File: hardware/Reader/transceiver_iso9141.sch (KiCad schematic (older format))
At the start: 8 parts

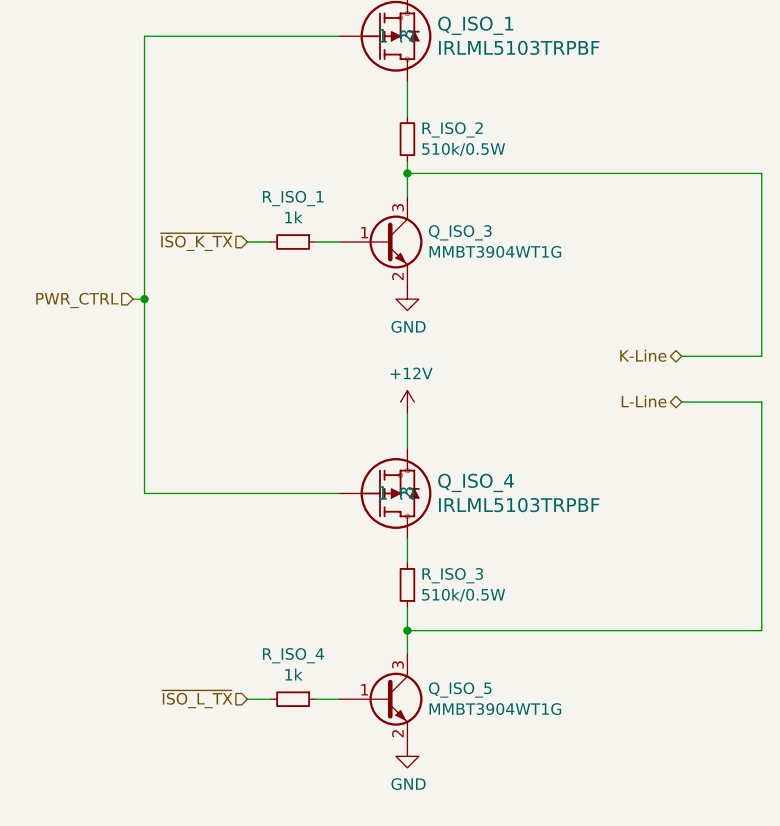
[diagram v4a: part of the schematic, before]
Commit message: Fixed bugs on the reader schematic. Exported Schematic Electrical report
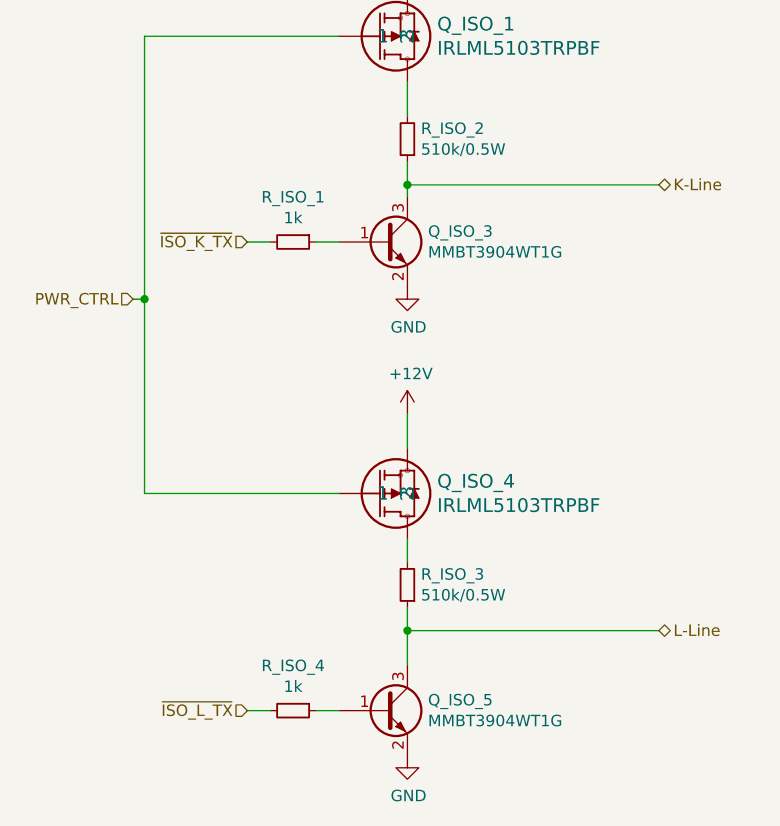
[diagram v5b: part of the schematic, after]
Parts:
- Q_ISO_1, Q_ISO_4: Manufacturer (none) -> Infineon Technologies; Part Name (none) -> IRLML5103TRPBF; Vendor (none) -> DigiKey Canada; digikeypn (none) -> IRLML5103PBFCT-ND
- Q_ISO_3, Q_ISO_5: Manufacturer (none) -> ON Semiconductor; Part Name (none) -> MMBT3904WT1G; Vendor (none) -> DigiKey Canada; digikeypn (none) -> MMBT3904WT1GOSCT-ND
- R_ISO_1, R_ISO_4: Manufacturer (none) -> Samsung Electro-Mechanics; Vendor (none) -> DigiKey Canada; digikeypn (none) -> 1276-3484-1-ND
- R_ISO_2, R_ISO_3: Manufacturer (none) -> Panasonic Electronic Components; Vendor (none) -> DigiKey Canada; digikeypn (none) -> P510KADCT-ND
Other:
- moved on the sheet: Q_ISO_5, R_ISO_4
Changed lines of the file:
@@
 $EndDescr
-Wire Wire Line
-	4450 2250 5300 2250
-Wire Wire Line
-	4450 3400 4450 2250
-Wire Wire Line
-	4400 3400 4450 3400
 Wire Wire Line
 	5600 2050 5600 1900
@@
 $EndComp
 Wire Wire Line
-	5600 2800 5600 2850
-Wire Wire Line
 	5600 2600 5600 2450
 $Comp
@@
 F 3 "https://industrial.panasonic.com/cdbs/www-data/pdf/RDO0000/AOA0000C331.pdf" H 5600 2700 50  0001 C CNN
 F 4 "ERJ-P06J514V" H 5600 2700 50  0001 C CNN "Part Name"
+F 5 "DigiKey Canada" H 5600 2700 50  0001 C CNN "Vendor"
+F 6 "Panasonic Electronic Components" H 5600 2700 50  0001 C CNN "Manufacturer"
+F 7 "P510KADCT-ND" H 5600 2700 50  0001 C CNN "digikeypn"
 	1    5600 2700
 	-1   0    0    1
@@
 F 3 "https://media.digikey.com/pdf/Data%20Sheets/Samsung%20PDFs/RC_Series_ds.pdf" H 5100 3150 50  0001 C CNN
 F 4 "RC1608F102CS" H 5100 3150 50  0001 C CNN "Part Name"
+F 5 "Samsung Electro-Mechanics" H 5100 3150 50  0001 C CNN "Manufacturer"
+F 6 "DigiKey Canada" H 5100 3150 50  0001 C CNN "Vendor"
+F 7 "1276-3484-1-ND" H 5100 3150 50  0001 C CNN "digikeypn"
 	1    5100 3150
 	0    1    1    0
@@
 L power:GND #PWR0126
 U 1 1 5FA99780
-P 5600 5350
-F 0 "#PWR0126" H 5600 5100 50  0001 C CNN
-F 1 "GND" H 5605 5177 50  0000 C CNN
-F 2 "" H 5600 5350 50  0001 C CNN
-F 3 "" H 5600 5350 50  0001 C CNN
-	1    5600 5350
+P 5600 5400
+F 0 "#PWR0126" H 5600 5150 50  0001 C CNN
+F 1 "GND" H 5605 5227 50  0000 C CNN
+F 2 "" H 5600 5400 50  0001 C CNN
+F 3 "" H 5600 5400 50  0001 C CNN
+	1    5600 5400
 	1    0    0    -1
 $EndComp
@@
 L Transistor_BJT:MMBT3904 Q_ISO_5
 U 1 1 5FA953EB
-P 5500 5150
-F 0 "Q_ISO_5" H 5690 5196 50  0000 L CNN
-F 1 "MMBT3904WT1G" H 5690 5105 50  0000 L CNN
-F 2 "Package_TO_SOT_SMD:SOT-23" H 5700 5075 50  0001 L CIN
-F 3 "https://www.onsemi.com/pub/Collateral/MMBT3904WT1-D.PDF" H 5500 5150 50  0001 L CNN
-	1    5500 5150
+P 5500 5200
+F 0 "Q_ISO_5" H 5690 5246 50  0000 L CNN
+F 1 "MMBT3904WT1G" H 5690 5155 50  0000 L CNN
+F 2 "Package_TO_SOT_SMD:SOT-23" H 5700 5125 50  0001 L CIN
+F 3 "https://www.onsemi.com/pub/Collateral/MMBT3904WT1-D.PDF" H 5500 5200 50  0001 L CNN
+F 4 "MMBT3904WT1G" H 5500 5200 50  0001 C CNN "Part Name"
+F 5 "DigiKey Canada" H 5500 5200 50  0001 C CNN "Vendor"
+F 6 "ON Semiconductor" H 5500 5200 50  0001 C CNN "Manufacturer"
+F 7 "MMBT3904WT1GOSCT-ND" H 5500 5200 50  0001 C CNN "digikeypn"
+	1    5500 5200
 	1    0    0    -1
 $EndComp
@@
 F 2 "Package_TO_SOT_SMD:SOT-23" H 5700 3075 50  0001 L CIN
 F 3 "https://www.onsemi.com/pub/Collateral/MMBT3904WT1-D.PDF" H 5500 3150 50  0001 L CNN
+F 4 "MMBT3904WT1G" H 5500 3150 50  0001 C CNN "Part Name"
+F 5 "DigiKey Canada" H 5500 3150 50  0001 C CNN "Vendor"
+F 6 "ON Semiconductor" H 5500 3150 50  0001 C CNN "Manufacturer"
+F 7 "MMBT3904WT1GOSCT-ND" H 5500 3150 50  0001 C CNN "digikeypn"
 	1    5500 3150
 	1    0    0    -1
@@
 F 3 "https://industrial.panasonic.com/cdbs/www-data/pdf/RDO0000/AOA0000C331.pdf" H 5600 4650 50  0001 C CNN
 F 4 "ERJ-P06J514V" H 5600 4650 50  0001 C CNN "Part Name"
+F 5 "DigiKey Canada" H 5600 4650 50  0001 C CNN "Vendor"
+F 6 "Panasonic Electronic Components" H 5600 4650 50  0001 C CNN "Manufacturer"
+F 7 "P510KADCT-ND" H 5600 4650 50  0001 C CNN "digikeypn"
 	1    5600 4650
 	-1   0    0    1
@@
 F 1 "IRLML5103TRPBF" H 5730 4303 60  0000 L CNN
 F 2 "footprints:IRLML5103TRPBF" H 5750 3990 60  0001 C CNN
-F 3 "" H 5300 4250 60  0000 C CNN
+F 3 "https://www.infineon.com/dgdl/irlml5103pbf.pdf?fileId=5546d462533600a401535668505d2617" H 5300 4250 60  0001 C CNN
+F 4 "IRLML5103TRPBF" H 5300 4250 50  0001 C CNN "Part Name"
+F 5 "DigiKey Canada" H 5300 4250 50  0001 C CNN "Vendor"
+F 6 "Infineon Technologies" H 5300 4250 50  0001 C CNN "Manufacturer"
+F 7 "IRLML5103PBFCT-ND" H 5300 4250 50  0001 C CNN "digikeypn"
 	1    5300 4250
 	1    0    0    1
@@
 F 1 "IRLML5103TRPBF" H 5730 2303 60  0000 L CNN
 F 2 "footprints:IRLML5103TRPBF" H 5750 1990 60  0001 C CNN
-F 3 "" H 5300 2250 60  0000 C CNN
+F 3 "https://www.infineon.com/dgdl/irlml5103pbf.pdf?fileId=5546d462533600a401535668505d2617" H 5300 2250 60  0001 C CNN
+F 4 "IRLML5103TRPBF" H 5300 2250 50  0001 C CNN "Part Name"
+F 5 "DigiKey Canada" H 5300 2250 50  0001 C CNN "Vendor"
+F 6 "Infineon Technologies" H 5300 2250 50  0001 C CNN "Manufacturer"
+F 7 "IRLML5103PBFCT-ND" H 5300 2250 50  0001 C CNN "digikeypn"
 	1    5300 2250
 	1    0    0    1
@@
 Text HLabel 4900 3150 0    50   Input ~ 0
 ~ISO_K_TX~
+Text HLabel 4900 5200 0    50   Input ~ 0
+~ISO_L_TX~
+$Comp
+L Device:R_Small R_ISO_4
+U 1 1 5FAABEED
+P 5100 5200
+F 0 "R_ISO_4" V 4904 5200 50  0000 C CNN
+F 1 "1k" V 4995 5200 50  0000 C CNN
+F 2 "footprints:RC1608F102CS" H 5100 5200 50  0001 C CNN
+F 3 "https://media.digikey.com/pdf/Data%20Sheets/Samsung%20PDFs/RC_Series_ds.pdf" H 5100 5200 50  0001 C CNN
+F 4 "RC1608F102CS" H 5100 5200 50  0001 C CNN "Part Name"
+F 5 "Samsung Electro-Mechanics" H 5100 5200 50  0001 C CNN "Manufacturer"
+F 6 "DigiKey Canada" H 5100 5200 50  0001 C CNN "Vendor"
+F 7 "1276-3484-1-ND" H 5100 5200 50  0001 C CNN "digikeypn"
+	1    5100 5200
+	0    1    1    0
+$EndComp
+Wire Wire Line
+	4900 5200 5000 5200
+Wire Wire Line
+	5200 5200 5300 5200
+Text HLabel 6700 2900 2    50   BiDi ~ 0
+K-Line
+Text HLabel 6700 4850 2    50   BiDi ~ 0
+L-Line
+Wire Wire Line
+	5600 2800 5600 2900
+Wire Wire Line
+	5600 4750 5600 4850
+Wire Wire Line
+	5600 2900 6700 2900
+Connection ~ 5600 2900
+Wire Wire Line
+	5600 2900 5600 2950
+Wire Wire Line
+	5600 4850 6700 4850
+Connection ~ 5600 4850
+Wire Wire Line
+	5600 4850 5600 5000
+Wire Wire Line
+	4450 4250 5300 4250
+Wire Wire Line
+	4450 2250 5300 2250
+Wire Wire Line
+	4450 3400 4450 2250
+Wire Wire Line
+	4400 3400 4450 3400
 Text HLabel 4400 3400 0    50   Input ~ 0
 PWR_CTRL
-Connection ~ 5600 2850
-Wire Wire Line
-	5600 2850 5600 2950
 Wire Wire Line
 	4450 3400 4450 4250
-Wire Wire Line
-	4450 4250 5300 4250
 Connection ~ 4450 3400
-Text HLabel 4900 5150 0    50   Input ~ 0
-~ISO_L_TX~
-$Comp
-L Device:R_Small R_ISO_4
-U 1 1 5FAABEED
-P 5100 5150
-F 0 "R_ISO_4" V 4904 5150 50  0000 C CNN
-F 1 "1k" V 4995 5150 50  0000 C CNN
-F 2 "footprints:RC1608F102CS" H 5100 5150 50  0001 C CNN
-F 3 "https://media.digikey.com/pdf/Data%20Sheets/Samsung%20PDFs/RC_Series_ds.pdf" H 5100 5150 50  0001 C CNN
-F 4 "RC1608F102CS" H 5100 5150 50  0001 C CNN "Part Name"
-	1    5100 5150
-	0    1    1    0
-$EndComp
-Wire Wire Line
-	4900 5150 5000 5150
-Wire Wire Line
-	5200 5150 5300 5150
-Text HLabel 6800 3650 0    50   BiDi ~ 0
-K-Line
-Wire Wire Line
-	5600 2850 7150 2850
-Connection ~ 5600 4850
-Wire Wire Line
-	5600 4750 5600 4850
-Wire Wire Line
-	5600 4850 5600 4950
-Text HLabel 6800 3850 0    50   BiDi ~ 0
-L-Line
-Wire Wire Line
-	6800 3650 7150 3650
-Wire Wire Line
-	5600 4850 7150 4850
-Wire Wire Line
-	7150 3850 6800 3850
-Wire Wire Line
-	7150 4850 7150 3850
-Wire Wire Line
-	7150 3650 7150 2850
 $EndSCHEMATC

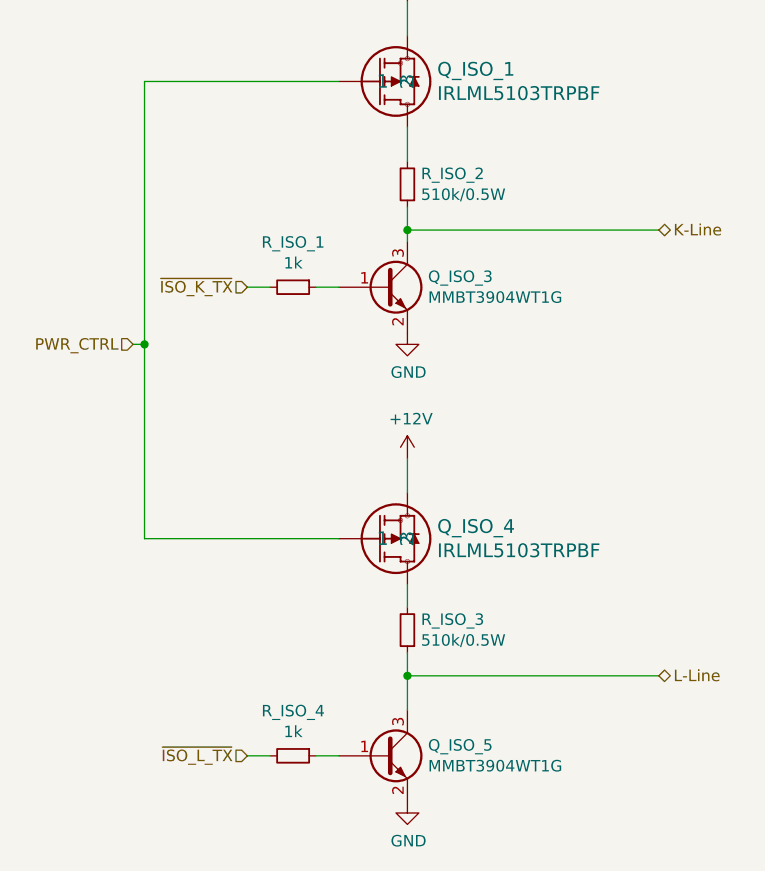
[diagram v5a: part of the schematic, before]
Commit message: Fixed wiring issue on ESD Protection
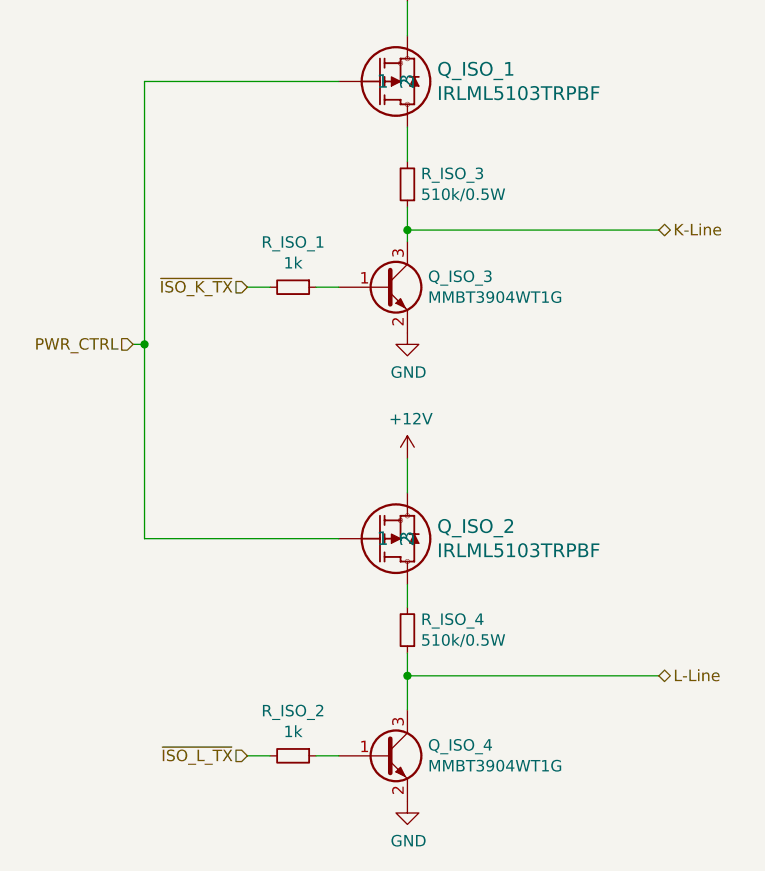
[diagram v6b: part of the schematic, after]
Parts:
- renumbered Q_ISO_4 to Q_ISO_2, Q_ISO_5 to Q_ISO_4, R_ISO_4 to R_ISO_2, R_ISO_2 to R_ISO_3, R_ISO_3 to R_ISO_4
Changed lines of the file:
@@
 	5600 2050 5600 1900
 $Comp
-L power:+12V #PWR0124
+L power:+12V #PWR011
 U 1 1 5FA9FF9E
 P 5600 1900
-F 0 "#PWR0124" H 5600 1750 50  0001 C CNN
+F 0 "#PWR011" H 5600 1750 50  0001 C CNN
 F 1 "+12V" H 5615 2073 50  0000 C CNN
 F 2 "" H 5600 1900 50  0001 C CNN
@@
 $EndComp
 $Comp
-L power:+12V #PWR0125
+L power:+12V #PWR013
 U 1 1 5FA9FB8D
 P 5600 3900
-F 0 "#PWR0125" H 5600 3750 50  0001 C CNN
+F 0 "#PWR013" H 5600 3750 50  0001 C CNN
 F 1 "+12V" H 5615 4073 50  0000 C CNN
 F 2 "" H 5600 3900 50  0001 C CNN
@@
 	5600 2600 5600 2450
 $Comp
-L Device:R_Small R_ISO_2
+L Device:R_Small R_ISO_3
 U 1 1 5FA9DCCB
 P 5600 2700
-F 0 "R_ISO_2" H 5541 2654 50  0000 R CNN
+F 0 "R_ISO_3" H 5541 2654 50  0000 R CNN
 F 1 "510k/0.5W" H 5541 2745 50  0000 R CNN
 F 2 "footprints:RESC2012X70N" H 5600 2700 50  0001 C CNN
@@
 $EndComp
 $Comp
-L power:GND #PWR0126
+L power:GND #PWR014
 U 1 1 5FA99780
 P 5600 5400
-F 0 "#PWR0126" H 5600 5150 50  0001 C CNN
+F 0 "#PWR014" H 5600 5150 50  0001 C CNN
 F 1 "GND" H 5605 5227 50  0000 C CNN
 F 2 "" H 5600 5400 50  0001 C CNN
@@
 $EndComp
 $Comp
-L power:GND #PWR0127
+L power:GND #PWR012
 U 1 1 5FA99363
 P 5600 3350
-F 0 "#PWR0127" H 5600 3100 50  0001 C CNN
+F 0 "#PWR012" H 5600 3100 50  0001 C CNN
 F 1 "GND" H 5605 3177 50  0000 C CNN
 F 2 "" H 5600 3350 50  0001 C CNN
@@
 	5600 4550 5600 4450
 $Comp
-L Transistor_BJT:MMBT3904 Q_ISO_5
+L Transistor_BJT:MMBT3904 Q_ISO_4
 U 1 1 5FA953EB
 P 5500 5200
-F 0 "Q_ISO_5" H 5690 5246 50  0000 L CNN
+F 0 "Q_ISO_4" H 5690 5246 50  0000 L CNN
 F 1 "MMBT3904WT1G" H 5690 5155 50  0000 L CNN
 F 2 "Package_TO_SOT_SMD:SOT-23" H 5700 5125 50  0001 L CIN
@@
 $EndComp
 $Comp
-L Device:R_Small R_ISO_3
+L Device:R_Small R_ISO_4
 U 1 1 5FA9021C
 P 5600 4650
-F 0 "R_ISO_3" H 5541 4604 50  0000 R CNN
+F 0 "R_ISO_4" H 5541 4604 50  0000 R CNN
 F 1 "510k/0.5W" H 5541 4695 50  0000 R CNN
 F 2 "footprints:RESC2012X70N" H 5600 4650 50  0001 C CNN
@@
 $EndComp
 $Comp
-L IRLML5103TRPBF:IRLML5103TRPBF Q_ISO_4
+L IRLML5103TRPBF:IRLML5103TRPBF Q_ISO_2
 U 1 1 5FA86CC3
 P 5300 4250
-F 0 "Q_ISO_4" H 5730 4197 60  0000 L CNN
+F 0 "Q_ISO_2" H 5730 4197 60  0000 L CNN
 F 1 "IRLML5103TRPBF" H 5730 4303 60  0000 L CNN
 F 2 "footprints:IRLML5103TRPBF" H 5750 3990 60  0001 C CNN
@@
 ~ISO_L_TX~
 $Comp
-L Device:R_Small R_ISO_4
+L Device:R_Small R_ISO_2
 U 1 1 5FAABEED
 P 5100 5200
-F 0 "R_ISO_4" V 4904 5200 50  0000 C CNN
+F 0 "R_ISO_2" V 4904 5200 50  0000 C CNN
 F 1 "1k" V 4995 5200 50  0000 C CNN
 F 2 "footprints:RC1608F102CS" H 5100 5200 50  0001 C CNN

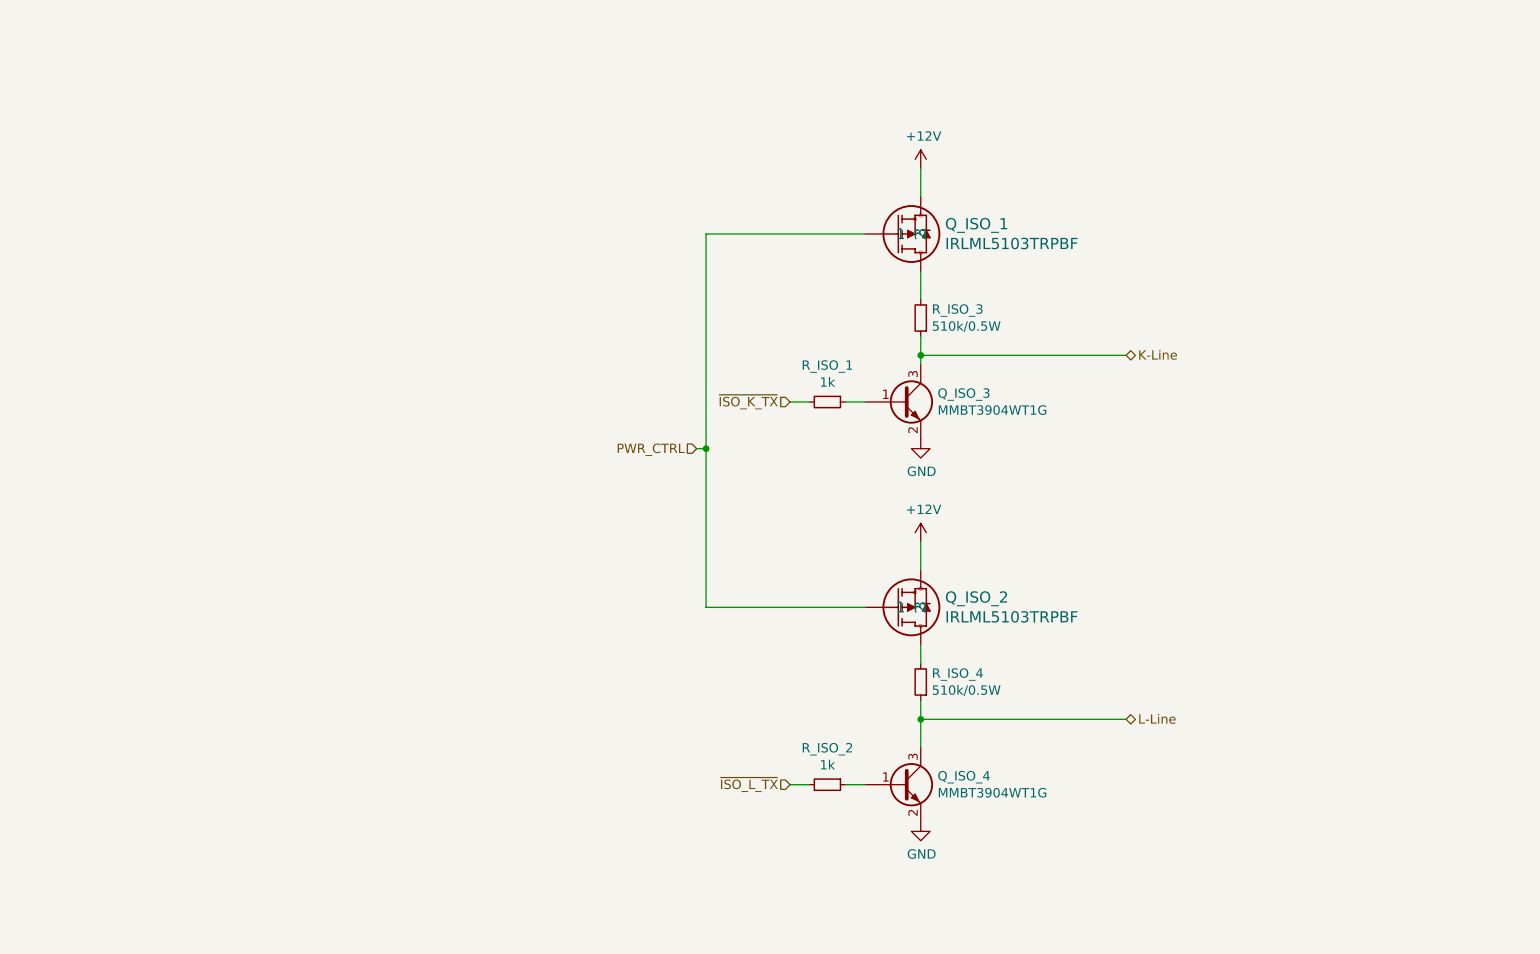
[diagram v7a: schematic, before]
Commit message: Fixed bugs in schematic. Updated BOM list. Swapped to using ESP32 holder. Updated PCB layout to v0.0.2. Updated schematic to v0.0.4
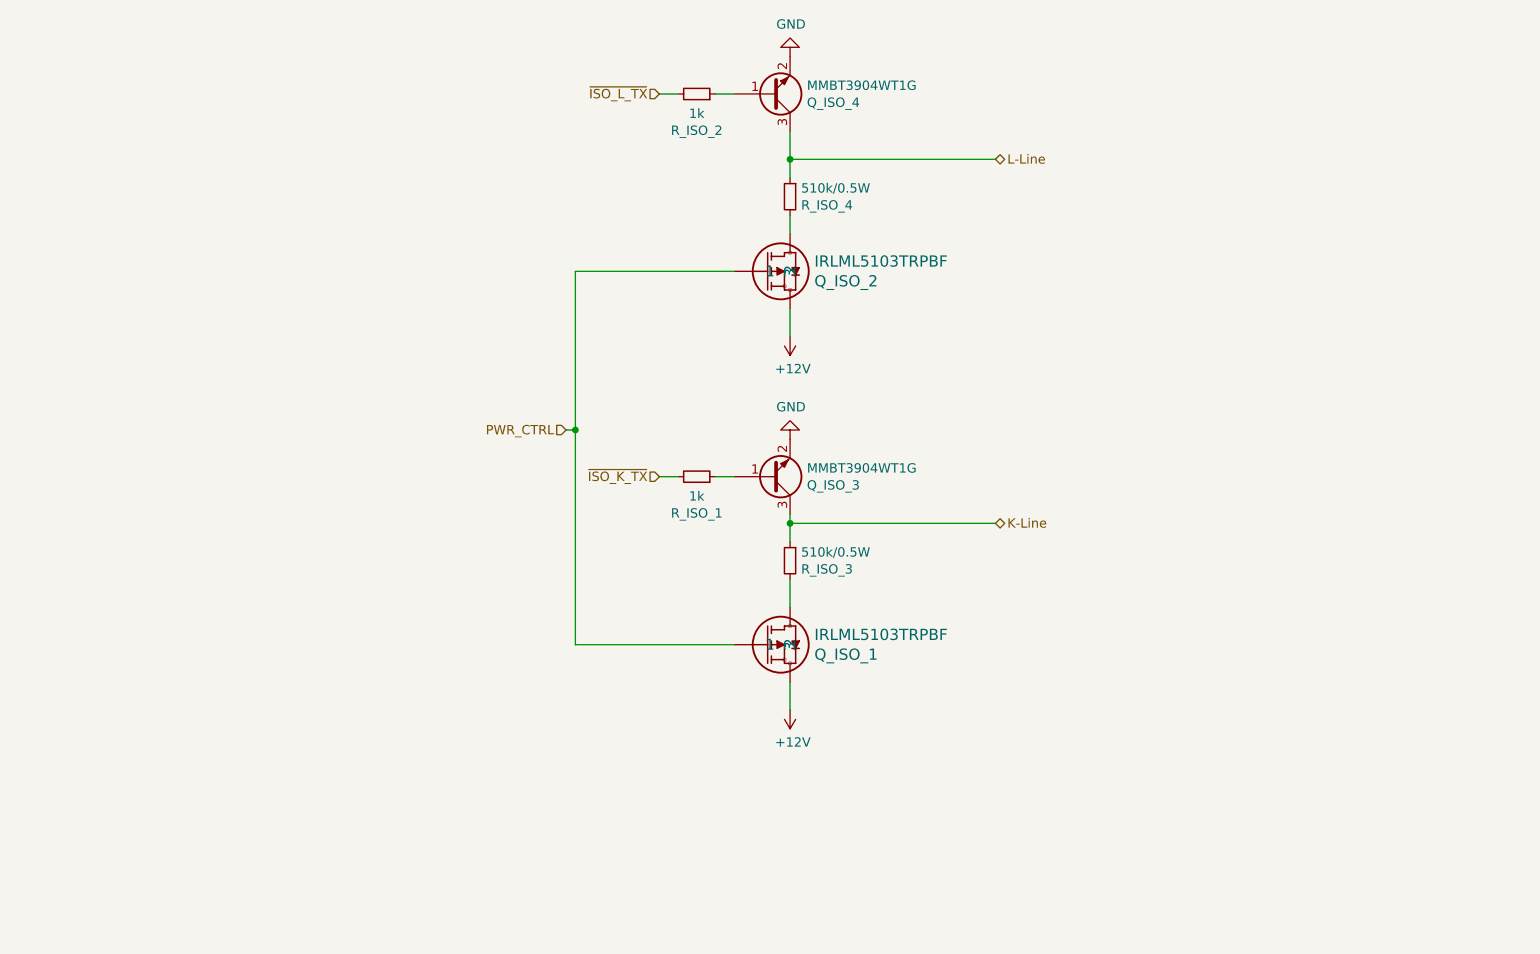
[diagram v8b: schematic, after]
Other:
- moved on the sheet: Q_ISO_1, Q_ISO_2, Q_ISO_3, Q_ISO_4, R_ISO_1, R_ISO_2, R_ISO_3, R_ISO_4
